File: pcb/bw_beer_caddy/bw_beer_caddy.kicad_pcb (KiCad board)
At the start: 2 copper layers, 70 x 64 mm, 38 parts, among them J1 Screw_Terminal_01x06, J3 Screw_Terminal_01x03, J4 Screw_Terminal_01x03, J5 Conn_01x03_Female, J6 Conn_01x03_Female, J7 Conn_02x04_Top_Bottom, J8 Conn_02x04_Top_Bottom, J9 Screw_Terminal_01x06, K1 G5LE-1, Q1 2N3904, Q2 FQP27P06, Q3 2N7000, Q4 2N3904, Q5 2N7000, U1 ina219_breakout, U2 LM2575-5.0BT, U3 LM2575-12BT, U4 LM2575-12BT, U5 LM2575-12BT, U6 SEN-13879

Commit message: bw_bcause rev 00 release
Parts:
- added D2: LED, LED_SMD:LED_1206_3216Metric, F.Cu at (149.0, 45.6)
- added D3: LED, LED_SMD:LED_1206_3216Metric, F.Cu at (155.0, 45.6)
- added D4: LED, LED_SMD:LED_1206_3216Metric, F.Cu at (161.0, 45.6)
- added J10: Conn_01x03_Female, Connector_PinHeader_2.54mm:PinHeader_1x03_P2.54mm_Vertical, F.Cu at (111.0, 101.0)
- added J2: Conn_01x03_Female, Connector_PinHeader_2.54mm:PinHeader_1x03_P2.54mm_Vertical, F.Cu at (120.0, 101.0)
- added R10: 10K, Resistor_SMD:R_0805_2012Metric, F.Cu at (149.0, 48.0)
- added R11: 10K, Resistor_SMD:R_0805_2012Metric, F.Cu at (155.0, 48.0)
- added R12: 10K, Resistor_SMD:R_0805_2012Metric, F.Cu at (161.0, 48.0)
- added R13: 10K, Resistor_SMD:R_0805_2012Metric, F.Cu at (146.0, 86.0)
- J3: value Screw_Terminal_01x03 -> Screw_Terminal_01x04; footprint TerminalBlock_TE-Connectivity:TerminalBlock_TE_282834-3_1x03_P2.54mm_Horizontal -> TerminalBlock_TE-Connectivity:TerminalBlock_TE_282834-4_1x04_P2.54mm_Horizontal
- J4: value Screw_Terminal_01x03 -> Screw_Terminal_01x05; footprint TerminalBlock_TE-Connectivity:TerminalBlock_TE_282834-3_1x03_P2.54mm_Horizontal -> TerminalBlock_TE-Connectivity:TerminalBlock_TE_282834-5_1x05_P2.54mm_Horizontal
- J7: value Conn_02x04_Top_Bottom -> Conn_02x08_Top_Bottom; footprint Connector_PinHeader_2.54mm:PinHeader_2x04_P2.54mm_Vertical -> Connector_PinHeader_2.54mm:PinHeader_2x08_P2.54mm_Vertical
- R8: value 6K -> 10K
- U3, U4, U5: value LM2575-12BT -> LM2576TV-012G; footprint Package_TO_SOT_THT:TO-220-5_Vertical -> Package_TO_SOT_THT:TO-220-5_P3.4x3.7mm_StaggerOdd_Lead3.8mm_Vertical
- moved R5 43.9 mm to (140.0, 98.0), turned to 180 degrees
- moved R1 43.1 mm to (134.0, 98.0), turned to 180 degrees
- moved R6 41.1 mm to (140.0, 94.0), turned to 180 degrees
- moved R8 39.8 mm to (140.0, 90.0), turned to 180 degrees
- moved R2 39.3 mm to (134.0, 94.0), turned to 180 degrees
- moved R3 36.1 mm to (134.0, 90.0), turned to 180 degrees
- moved D1 35.7 mm to (143.6, 49.0), turned to 180 degrees
- moved R9 34.9 mm to (140.0, 86.0), turned to 180 degrees
- moved R4 33.2 mm to (134.0, 86.0), turned to 180 degrees
- moved U1 31.1 mm to (126.7, 75.1), turned to 180 degrees
- moved U4 30.2 mm to (164.3, 87.6)
- moved U$2 28.6 mm to (129.8, 62.0)
- moved U3 26.3 mm to (164.3, 63.6)
- moved U6 24.7 mm to (143.3, 88.0)
- moved C1 23.6 mm to (110.8, 92.4)
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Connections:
- J3 pad 3: /MAIN_SWT_OUT -> Net-(J3-Pad1)
- J4 pad 3: /LED_RING -> +5V
- J7 pad 1: /M1_EA -> +3.3V
- J7 pad 2: /M1_EB -> /M1_EA
- J7 pad 3: /M2_EA -> /M1_EB
- J7 pad 4: /M2_EA -> GND
- J7 pad 5: /M3_EA -> +3.3V
- J7 pad 6: /M3_EB -> /M2_EA
- J7 pad 7: /M4_EA -> /M2_EA
- J7 pad 8: /M4_EB -> GND
- U$2 pad 17/A3: unconnected-(U$2-Pad17/A3) -> /HALL_EFFECT_SNS
- U$2 pad 20/A6: /M2_EB -> /M4_DR2
- U$2 pad 21/A7: /M2_EA -> /M4_DR1
- U$2 pad 22/A8: /M1_EB -> /M3_DR2
- U$2 pad 23/A9: /M1_EA -> /M3_DR1
- U$2 pad 24: /UNLATCH -> /M3_EA
- U$2 pad 25: /LATCH_STAT -> /M3_EB
- U$2 pad 26: unconnected-(U$2-Pad26) -> /M4_EA
- U$2 pad 27: /M3_DR1 -> /M4_EB
- U$2 pad 28: /M3_DR2 -> unconnected-(U$2-Pad28)
- U$2 pad 29: /M4_DR1 -> /CHARGE_RELAY_CTRL
- U$2 pad 3/CANTX: /M3_EA -> /M1_EA
- U$2 pad 30: /M4_DR2 -> /UNLATCH
- U$2 pad 31/A12: unconnected-(U$2-Pad31/A12) -> /LATCH_STAT
- U$2 pad 32/A13: unconnected-(U$2-Pad32/A13) -> /STATUS_LED
- U$2 pad 33/A14: /RX_JETSON -> /MOTOR_ENABLE
- U$2 pad 34/A15: /TX_JETSON -> /USB_SENSE
- U$2 pad 4/CANRX: /M3_EB -> /M1_EB
- U$2 pad 5: /M4_EA -> /M2_EA
- U$2 pad 6: /M4_EB -> /M2_EB
- U$2 pad 7: /USB_SENSE -> /RX_JETSON
- U$2 pad 8: /MOTOR_ENABLE -> /TX_JETSON
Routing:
- net GND: track 0.00 -> 465.3 mm, vias 0 -> 17
- net /M3_DR1: track 7.56 -> 90.5 mm, vias 0 -> 1
- net /HALL_EFFECT_SNS: track 0.00 -> 80.8 mm, vias 0 -> 1
- net /LED_RING: track 39.1 -> 119.3 mm
- net +3.3V: track 113.7 -> 191.3 mm, vias 1 -> 2
- net VDD: track 36.0 -> 111.7 mm
- net /M3_DR2: track 6.68 -> 79.2 mm, vias 0 -> 2
- net /M4_DR1: track 8.61 -> 80.0 mm
- net /MAIN_SWT_OUT: track 124.5 -> 54.7 mm, vias 1 -> 2
- net /M4_DR2: track 9.03 -> 78.6 mm
- net /E-: track 118.0 -> 57.1 mm
- net +12L: track 42.1 -> 102.4 mm
- net /BUTTON_LED: track 36.7 -> 87.0 mm
- net /M2_DR1: track 26.9 -> 72.8 mm
- net /M2_DR2: track 24.8 -> 69.5 mm, vias 0 -> 2
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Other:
- board size 70 x 64 mm -> 70 x 70 mm
- board text added: "Ben Warwick 2022"
- board text added: "bw_bcause Rev 00"

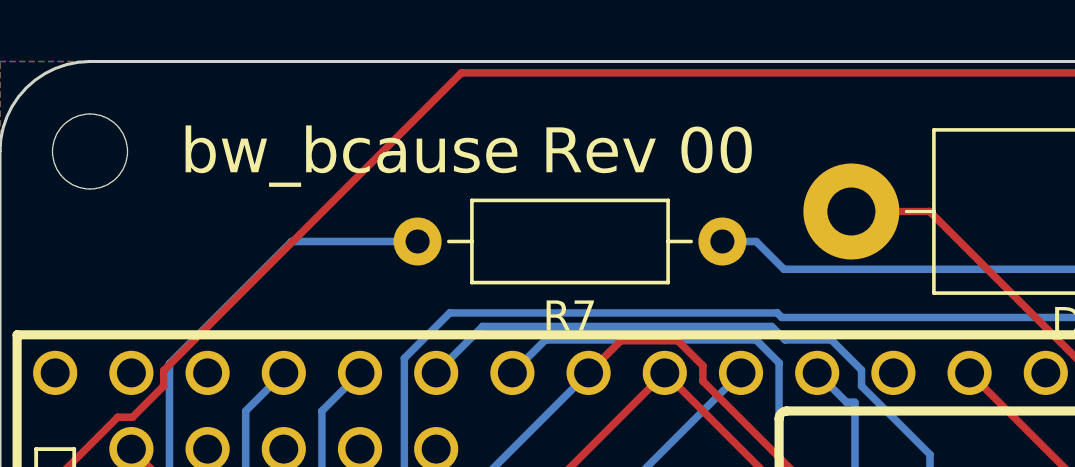
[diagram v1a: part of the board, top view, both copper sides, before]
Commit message: add servo test command
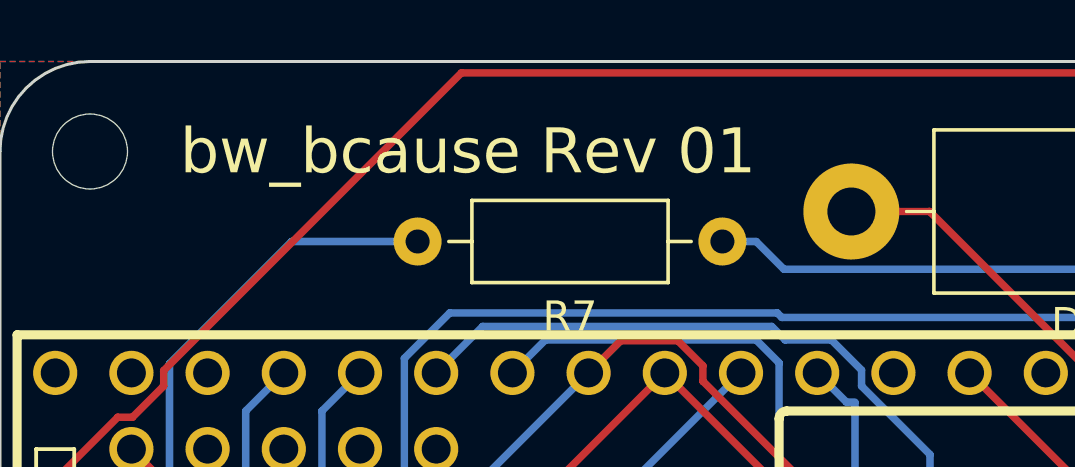
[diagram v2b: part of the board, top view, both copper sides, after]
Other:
- board text added: "bw_bcause Rev 01"
- board text removed: "bw_bcause Rev 00"
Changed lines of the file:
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@@
   (title_block
     (title "bw_beer_caddy")
-    (rev "0")
+    (rev "1")
     (company "BWBots")
   )
@@
     (effects (font (size 1.5 1.5) (thickness 0.3)) (justify left mirror))
   )
-  (gr_text "bw_bcause Rev 00" (at 106 47) (layer "F.SilkS")
+  (gr_text "bw_bcause Rev 01" (at 106 47) (layer "F.SilkS")
     (effects (font (size 1.5 1.5) (thickness 0.3)) (justify left))
   )

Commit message: pcb rev 01 08-21-2022
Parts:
- removed C1, C2: 22 UF, Capacitor_THT:C_Disc_D5.0mm_W2.5mm_P5.00mm
- removed the D1 at (143.6, 49.0)
- removed Hole1, Hole2, Hole3, Hole4: MountingHole_2.5mm, MountingHole:MountingHole_2.5mm
- removed K1: G5LE-1, Relay_THT:Relay_SPDT_Omron-G5LE-1
- removed Q1, Q4: 2N3904, Package_TO_SOT_THT:TO-92_Inline
- removed Q2: FQP27P06, Package_TO_SOT_THT:TO-220-3_Vertical
- removed Q3, Q5: 2N7000, Package_TO_SOT_THT:TO-92_Inline
- removed the R1 at (134.0, 98.0)
- removed R13, R4, R5, R8, R9: 10K, Resistor_SMD:R_0805_2012Metric
- removed the R2 at (134.0, 94.0)
- removed the R3 at (134.0, 90.0)
- removed R6: 100K, Resistor_SMD:R_0805_2012Metric
- removed R7: 10 Ohm, Resistor_THT:R_Axial_DIN0207_L6.3mm_D2.5mm_P10.16mm_Horizontal
- removed U$1: PCA9685, bwbots:PCA9685
- removed U4, U5: LM2576TV-012G, Package_TO_SOT_THT:TO-220-5_P3.4x3.7mm_StaggerOdd_Lead3.8mm_Vertical
- removed U6: SEN-13879, bwbots:SPARKFUN_SEN-13879
- added J11: Conn_01x03_Female, Connector_JST:JST_XH_B3B-XH-A_1x03_P2.50mm_Vertical, F.Cu at (166.0, 71.0)
- added J12: Conn_01x04_Female, Connector_JST:JST_XH_B4B-XH-A_1x04_P2.50mm_Vertical, F.Cu at (166.0, 84.5)
- added J13: Conn_01x03_Female, Connector_JST:JST_XH_B3B-XH-A_1x03_P2.50mm_Vertical, F.Cu at (166.0, 95.5)
- added J14: Conn_01x02_Female, Connector_PinHeader_2.54mm:PinHeader_1x02_P2.54mm_Vertical, F.Cu at (114.0, 74.0)
- added J15: Conn_01x02_Female, TerminalBlock_4Ucon:TerminalBlock_4Ucon_1x02_P3.50mm_Horizontal, F.Cu at (166.0, 104.8)
- added REF**: MountingHole_2.5mm, MountingHole:MountingHole_2.5mm, F.Cu at (103.0, 47.0)
- added REF**: MountingHole_2.5mm, MountingHole:MountingHole_2.5mm, F.Cu at (103.0, 111.0)
- added REF**: MountingHole_2.5mm, MountingHole:MountingHole_2.5mm, F.Cu at (167.0, 111.0)
- added REF**: MountingHole_2.5mm, MountingHole:MountingHole_2.5mm, F.Cu at (167.0, 47.0)
- D1: renamed from D2; moved to B.Cu
- D2: renamed from D3; moved to B.Cu
- D3: renamed from D4; moved to B.Cu
- J1, J9: value Screw_Terminal_01x06 -> Conn_01x04_Female; footprint TerminalBlock_TE-Connectivity:TerminalBlock_TE_282834-6_1x06_P2.54mm_Horizontal -> Connector_JST:JST_XH_B4B-XH-A_1x04_P2.50mm_Vertical
- J10, J5, J6: footprint Connector_PinHeader_2.54mm:PinHeader_1x03_P2.54mm_Vertical -> Connector_JST:JST_XH_B3B-XH-A_1x03_P2.50mm_Vertical
- J2: value Conn_01x03_Female -> Conn_01x04_Female; footprint Connector_PinHeader_2.54mm:PinHeader_1x03_P2.54mm_Vertical -> Connector_JST:JST_XH_B4B-XH-A_1x04_P2.50mm_Vertical
- J3: value Screw_Terminal_01x04 -> Conn_01x04_Female; footprint TerminalBlock_TE-Connectivity:TerminalBlock_TE_282834-4_1x04_P2.54mm_Horizontal -> Connector_JST:JST_XH_B4B-XH-A_1x04_P2.50mm_Vertical
- J4: value Screw_Terminal_01x05 -> Conn_01x04_Female; footprint TerminalBlock_TE-Connectivity:TerminalBlock_TE_282834-5_1x05_P2.54mm_Horizontal -> Connector_JST:JST_XH_B4B-XH-A_1x04_P2.50mm_Vertical
- J7: value Conn_02x08_Top_Bottom -> Conn_01x03_Female; footprint Connector_PinHeader_2.54mm:PinHeader_2x08_P2.54mm_Vertical -> Connector_JST:JST_XH_B3B-XH-A_1x03_P2.50mm_Vertical
- J8: value Conn_02x04_Top_Bottom -> Conn_01x04_Female; footprint Connector_PinHeader_2.54mm:PinHeader_2x04_P2.54mm_Vertical -> Connector_JST:JST_XH_B4B-XH-A_1x04_P2.50mm_Vertical
- R1: renamed from R10; moved to B.Cu
- R2: renamed from R11; moved to B.Cu
- R3: renamed from R12; moved to B.Cu
- U1: value ina219_breakout -> Pololu_5V_Step_Down_2851; footprint bwbots:ina219_breakout -> bwbots:Pololu_5V_Step_Down_2851; moved to F.Cu
- U2: value LM2575-5.0BT -> Pololu-MC33926-Dual-Motor; footprint Package_TO_SOT_THT:TO-220-5_Vertical -> bwbots:Pololu-MC33926-Dual-Motor-Vertical
- U3: value LM2576TV-012G -> Pololu-MC33926-Dual-Motor; footprint Package_TO_SOT_THT:TO-220-5_P3.4x3.7mm_StaggerOdd_Lead3.8mm_Vertical -> bwbots:Pololu-MC33926-Dual-Motor-Vertical
- moved J10 68.6 mm to (166.0, 60.0)
- moved J1 61.7 mm to (104.2, 80.0), turned to 0 degrees
- moved U2 54.7 mm to (136.0, 98.8), turned to 0 degrees
- moved U3 54.4 mm to (122.9, 98.8), turned to 0 degrees
- moved J4 36.3 mm to (104.2, 103.0), turned to 0 degrees
- moved U$2 27.1 mm to (153.0, 76.0), turned to 90 degrees
- moved J2 20.9 mm to (104.0, 87.5), turned to 0 degrees
- moved R3 18.9 mm to (142.1, 49.0), turned to 0 degrees
- moved D3 18.4 mm to (142.6, 45.6), turned to 180 degrees
- moved J8 12.1 mm to (118.5, 102.5), turned to 0 degrees
- moved J9 11.7 mm to (132.0, 102.5), turned to 0 degrees
- moved J7 11.2 mm to (132.0, 110.0), turned to 0 degrees
- moved J3 10.1 mm to (104.2, 95.0), turned to 0 degrees
- moved U1 9.12 mm to (118.1, 72.3), turned to 90 degrees
- moved D1 8.40 mm to (157.4, 45.6), turned to 180 degrees
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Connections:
- J1 pad 1: /BUTTON_LED -> unconnected-(J1-Pad1)
- J1 pad 2: GND -> unconnected-(J1-Pad2)
- J1 pad 3: /LATCH_BTN_IN -> unconnected-(J1-Pad3)
- J1 pad 4: /LATCH_BTN_OUT -> unconnected-(J1-Pad4)
- J10 pad 1: /HALL_EFFECT_SNS -> unconnected-(J10-Pad1)
- J10 pad 2: GND -> unconnected-(J10-Pad2)
- J10 pad 3: +3.3V -> unconnected-(J10-Pad3)
- J2 pad 1: /TX_JETSON -> unconnected-(J2-Pad1)
- J2 pad 2: /RX_JETSON -> unconnected-(J2-Pad2)
- J2 pad 3: GND -> unconnected-(J2-Pad3)
- J3 pad 1: Net-(J3-Pad1) -> unconnected-(J3-Pad1)
- J3 pad 2: GND -> unconnected-(J3-Pad2)
- J3 pad 3: Net-(J3-Pad1) -> unconnected-(J3-Pad3)
- J3 pad 4: GND -> unconnected-(J3-Pad4)
- J4 pad 1: +5V -> unconnected-(J4-Pad1)
- J4 pad 2: GND -> unconnected-(J4-Pad2)
- J4 pad 3: +5V -> unconnected-(J4-Pad3)
- J4 pad 4: GND -> unconnected-(J4-Pad4)
- J7 pad 1: +3.3V -> unconnected-(J7-Pad1)
- J7 pad 2: /M1_EA -> unconnected-(J7-Pad2)
- J7 pad 3: /M1_EB -> unconnected-(J7-Pad3)
- J8 pad 1: /M1_DR1 -> unconnected-(J8-Pad1)
- J8 pad 2: /M1_DR2 -> unconnected-(J8-Pad2)
- J8 pad 3: /M2_DR1 -> unconnected-(J8-Pad3)
- J8 pad 4: /M2_DR2 -> unconnected-(J8-Pad4)
- J9 pad 1: GND -> unconnected-(J9-Pad1)
- J9 pad 2: +12V -> unconnected-(J9-Pad2)
- J9 pad 3: GND -> unconnected-(J9-Pad3)
- J9 pad 4: +12V -> unconnected-(J9-Pad4)
- U$2 pad 14/A0: /BUTTON_LED -> unconnected-(U$2-Pad14/A0)
- U$2 pad 16/A2: /LOAD_CELL_SCK -> unconnected-(U$2-Pad16/A2)
- U$2 pad 17/A3: /HALL_EFFECT_SNS -> unconnected-(U$2-Pad17/A3)
- U$2 pad 18/A4/SDA: /SDA1 -> unconnected-(U$2-Pad18/A4/SDA)
- U$2 pad 19/A5/SCL: /SCL1 -> unconnected-(U$2-Pad19/A5/SCL)
- U$2 pad 2: /LOAD_CELL_DATA -> unconnected-(U$2-Pad2)
- U$2 pad 20/A6: /M4_DR2 -> unconnected-(U$2-Pad20/A6)
- U$2 pad 21/A7: /M4_DR1 -> unconnected-(U$2-Pad21/A7)
- U$2 pad 22/A8: /M3_DR2 -> unconnected-(U$2-Pad22/A8)
- U$2 pad 23/A9: /M3_DR1 -> unconnected-(U$2-Pad23/A9)
- U$2 pad 24: /M3_EA -> unconnected-(U$2-Pad24)
- U$2 pad 25: /M3_EB -> unconnected-(U$2-Pad25)
- U$2 pad 26: /M4_EA -> unconnected-(U$2-Pad26)
- U$2 pad 27: /M4_EB -> unconnected-(U$2-Pad27)
- U$2 pad 29: /CHARGE_RELAY_CTRL -> unconnected-(U$2-Pad29)
- U$2 pad 3/CANTX: /M1_EA -> unconnected-(U$2-Pad3/CANTX)
- U$2 pad 30: /UNLATCH -> unconnected-(U$2-Pad30)
- U$2 pad 31/A12: /LATCH_STAT -> unconnected-(U$2-Pad31/A12)
- U$2 pad 32/A13: /STATUS_LED -> unconnected-(U$2-Pad32/A13)
- U$2 pad 33/A14: /MOTOR_ENABLE -> unconnected-(U$2-Pad33/A14)
- U$2 pad 34/A15: /USB_SENSE -> unconnected-(U$2-Pad34/A15)
- U$2 pad 35/A16: /M2_DR2 -> unconnected-(U$2-Pad35/A16)
- U$2 pad 36/A17: /M2_DR1 -> unconnected-(U$2-Pad36/A17)
- U$2 pad 37/A18: /M1_DR2 -> unconnected-(U$2-Pad37/A18)
- U$2 pad 38/A19: /M1_DR1 -> unconnected-(U$2-Pad38/A19)
- U$2 pad 39/A20: /LED_RING -> unconnected-(U$2-Pad39/A20)
- U$2 pad 3V3: +3.3V -> unconnected-(U$2-Pad3V3)
- U$2 pad 4/CANRX: /M1_EB -> unconnected-(U$2-Pad4/CANRX)
- U$2 pad 5: /M2_EA -> unconnected-(U$2-Pad5)
- U$2 pad 6: /M2_EB -> unconnected-(U$2-Pad6)
- U$2 pad 7: /RX_JETSON -> unconnected-(U$2-Pad7)
- U$2 pad 8: /TX_JETSON -> unconnected-(U$2-Pad8)
- U$2 pad GND: GND -> unconnected-(U$2-PadGND)
- U$2 pad VUSB: Net-(R8-Pad2) -> unconnected-(U$2-PadVUSB)
- U1 pad 1: +3.3V -> unconnected-(U1-Pad1)
- U1 pad 2: GND -> unconnected-(U1-Pad2)
- U1 pad 3: /SCL1 -> unconnected-(U1-Pad3)
- U1 pad 4: /SDA1 -> unconnected-(U1-Pad4)
- U2 pad 1: VDD -> unconnected-(U2-Pad1)
- U2 pad 2: +5V -> unconnected-(U2-Pad2)
- U2 pad 3: GND -> unconnected-(U2-Pad3)
- U3 pad 1: VDD -> unconnected-(U3-Pad1)
- U3 pad 2: +12L -> unconnected-(U3-Pad2)
- U3 pad 3: GND -> unconnected-(U3-Pad3)
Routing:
- net GND: track 465.3 -> 0.00 mm, vias 17 -> 0
- net +3.3V: track 191.3 -> 0.00 mm, vias 2 -> 0
- net /MOTOR_ENABLE: track 140.9 -> 0.00 mm
- net +5V: track 130.6 -> 0.00 mm
- net /LED_RING: track 119.3 -> 0.00 mm, vias 1 -> 0
- net VDD: track 111.7 -> 0.00 mm
- net Net-(C1-Pad1): track 104.0 -> 0.00 mm, vias 1 -> 0
- net +12L: track 102.4 -> 0.00 mm, vias 1 -> 0
- net /SDA1: track 101.4 -> 0.00 mm, vias 1 -> 0
- net /SCL1: track 95.1 -> 0.00 mm, vias 1 -> 0
- net /M3_DR1: track 90.5 -> 0.00 mm, vias 1 -> 0
- net /LATCH_OUT: track 88.7 -> 0.00 mm, vias 2 -> 0
- net /M2_EA: track 88.5 -> 0.00 mm
- net /BUTTON_LED: track 87.0 -> 0.00 mm
- net +12V: track 86.6 -> 0.00 mm
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- removed copper zone on B.Cu, net GND
- removed copper zone on F.Cu, net GND

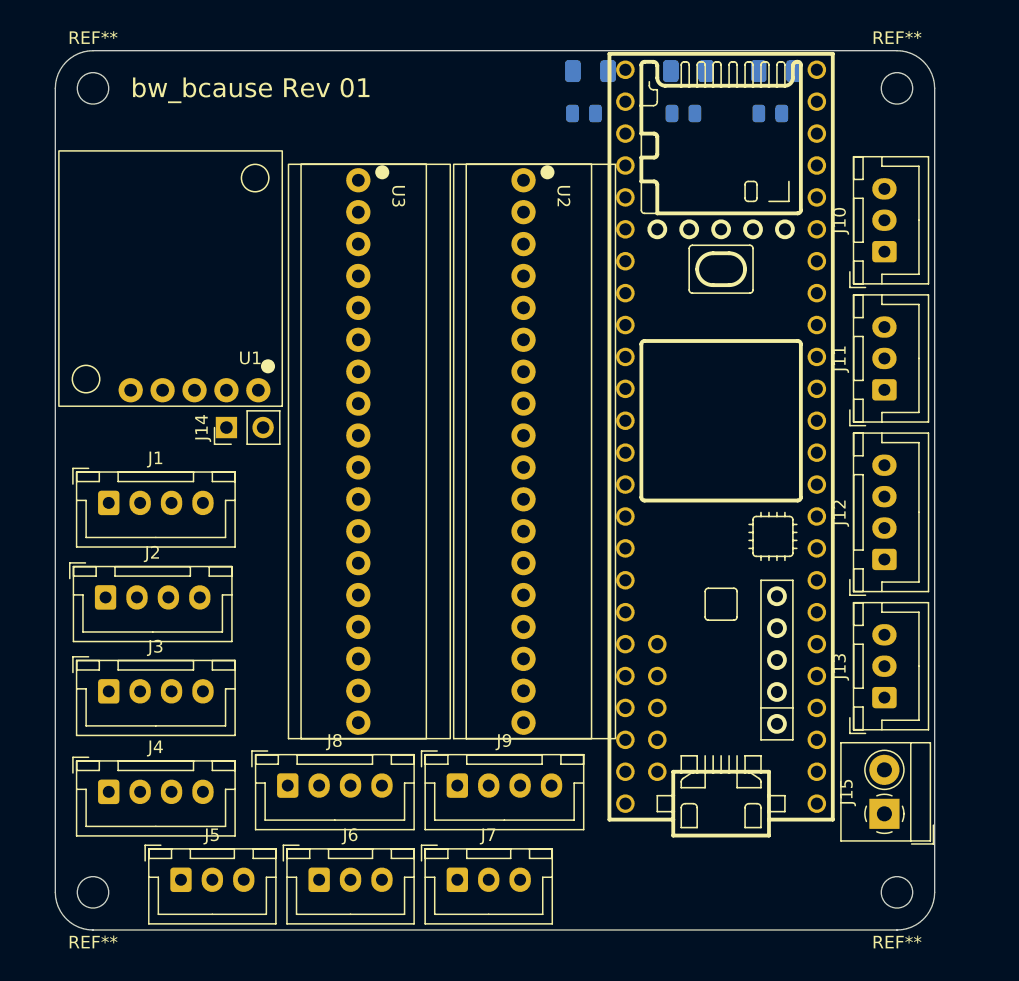
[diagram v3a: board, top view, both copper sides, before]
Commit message: rev 01 - fixing connectors
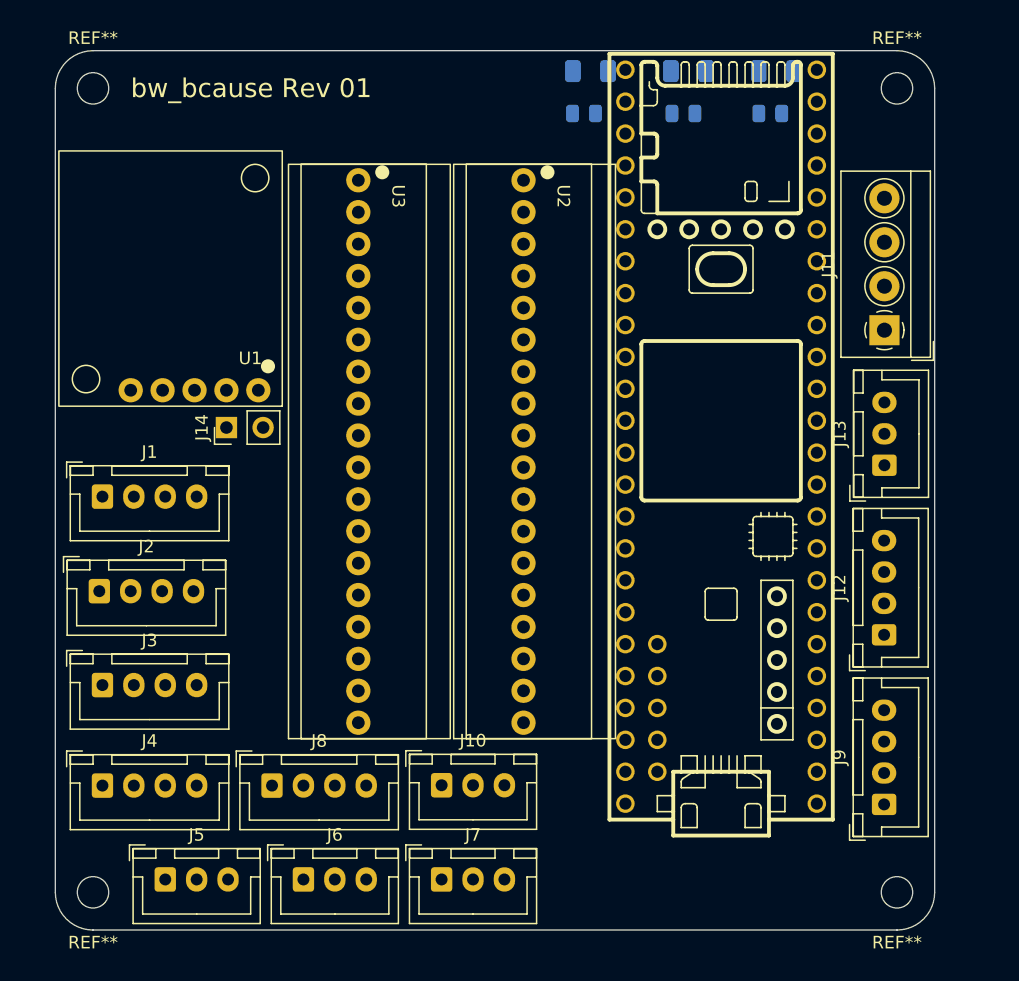
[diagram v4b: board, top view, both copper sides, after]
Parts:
- removed J15: Conn_01x02_Female, TerminalBlock_4Ucon:TerminalBlock_4Ucon_1x02_P3.50mm_Horizontal
- J11: value Conn_01x03_Female -> Conn_01x04_Female; footprint Connector_JST:JST_XH_B3B-XH-A_1x03_P2.50mm_Vertical -> TerminalBlock_4Ucon:TerminalBlock_4Ucon_1x04_P3.50mm_Horizontal
- moved J10 55.2 mm to (130.8, 102.5), turned to 0 degrees
- moved J9 34.0 mm to (166.0, 104.0), turned to 90 degrees
- moved J13 18.5 mm to (166.0, 77.0)
- moved J12 6.00 mm to (166.0, 90.5)
- moved J11 4.75 mm to (166.0, 66.2)
- moved J5 1.25 mm to (108.8, 110.0)
- moved J6 1.25 mm to (119.8, 110.0)
- moved J7 1.25 mm to (130.8, 110.0)
- moved J8 1.25 mm to (117.2, 102.5)
- moved J1 0.71 mm to (103.8, 79.5)
- moved J2 0.71 mm to (103.5, 87.0)
- moved J3 0.71 mm to (103.8, 94.5)
- moved J4 0.71 mm to (103.8, 102.5)

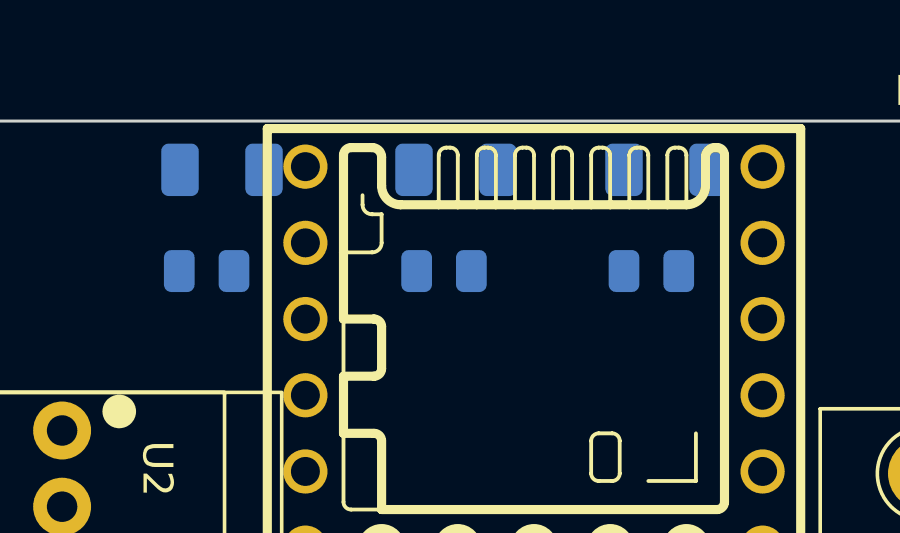
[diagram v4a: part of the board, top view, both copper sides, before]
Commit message: moving leds
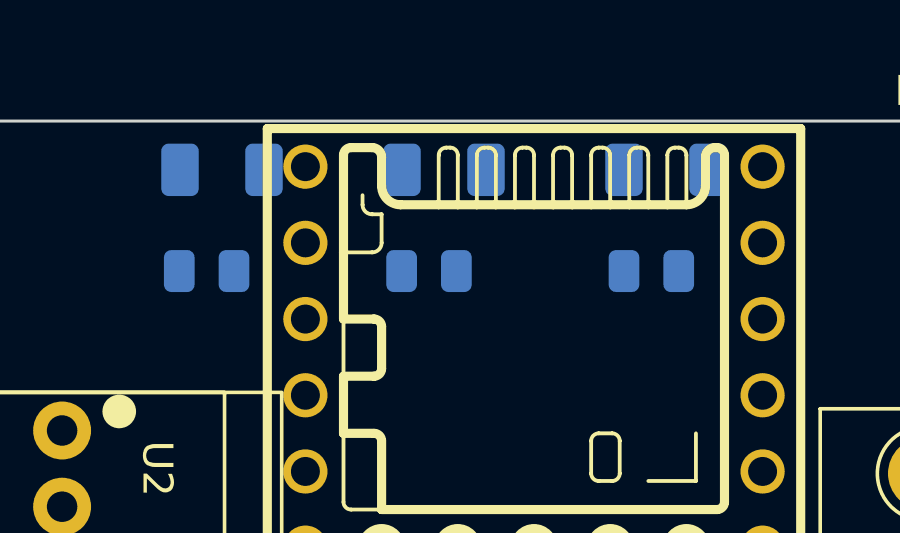
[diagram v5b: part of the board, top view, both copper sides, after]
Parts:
- moved R2 0.50 mm to (149.5, 49.0)
- moved D2 0.40 mm to (150.0, 45.6)
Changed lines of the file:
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@@
   )
   (footprint "LED_SMD:LED_1206_3216Metric" (layer "B.Cu")
-    (at 150.4 45.625 180)
+    (at 150 45.625 180)
     (descr "LED SMD 1206 (3216 Metric), square (rectangular) end terminal, IPC_7351 nominal, (Body size source: http://www.tortai-tech.com/upload/download/2011102023233369053.pdf), generated with kicad-footprint-generator")
     (tags "LED")
@@
   )
   (footprint "Resistor_SMD:R_0805_2012Metric" (layer "B.Cu")
-    (at 150 49)
+    (at 149.5 49)
     (descr "Resistor SMD 0805 (2012 Metric), square (rectangular) end terminal, IPC_7351 nominal, (Body size source: IPC-SM-782 page 72, https://www.pcb-3d.com/wordpress/wp-content/uploads/ipc-sm-782a_amendment_1_and_2.pdf), generated with kicad-footprint-generator")
     (tags "resistor")
